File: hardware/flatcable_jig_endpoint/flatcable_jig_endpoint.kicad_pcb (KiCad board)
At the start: 2 copper layers, 2 parts

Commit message: started layout, still need to add the endpad connections
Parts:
- added C1: C, SquantorRcl:C_0805, B.Cu at (111.5, 101.0)
- added C2: C, SquantorRcl:C_0805, B.Cu at (111.5, 108.0)
- added J3: Conn_01x03, Connector_Molex:Molex_KK-254_AE-6410-03A_1x03_P2.54mm_Vertical, F.Cu at (109.0, 104.0)
- added J4: Conn_01x03, Connector_Molex:Molex_KK-254_AE-6410-03A_1x03_P2.54mm_Vertical, F.Cu at (109.0, 111.0)
- added J5: Conn_02x05_Odd_Even, SquantorConnectors:Header-0254-2X05-H010, F.Cu at (126.0, 111.0)
- added R1: R, SquantorRcl:R_0603_hand, B.Cu at (117.0, 111.2)
- added R2: R, SquantorRcl:R_0603_hand, B.Cu at (117.0, 114.2)
- added R3: R, SquantorRcl:R_0603_hand, B.Cu at (117.0, 117.2)
- added R4: R, SquantorRcl:R_0603_hand, B.Cu at (119.5, 110.8)
- added R5: R, SquantorRcl:R_0603_hand, B.Cu at (119.5, 113.8)
- added R6: R, SquantorRcl:R_0603_hand, B.Cu at (119.5, 116.8)
- added R7: R, SquantorRcl:R_0603_hand, B.Cu at (122.0, 111.2)
- added R8: R, SquantorRcl:R_0603_hand, B.Cu at (122.0, 114.2)
- added R9: R, SquantorRcl:R_0603_hand, B.Cu at (122.0, 117.2)
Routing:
- added copper zone on F.Cu, net GND
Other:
- board outline added: 30 x 22 mm

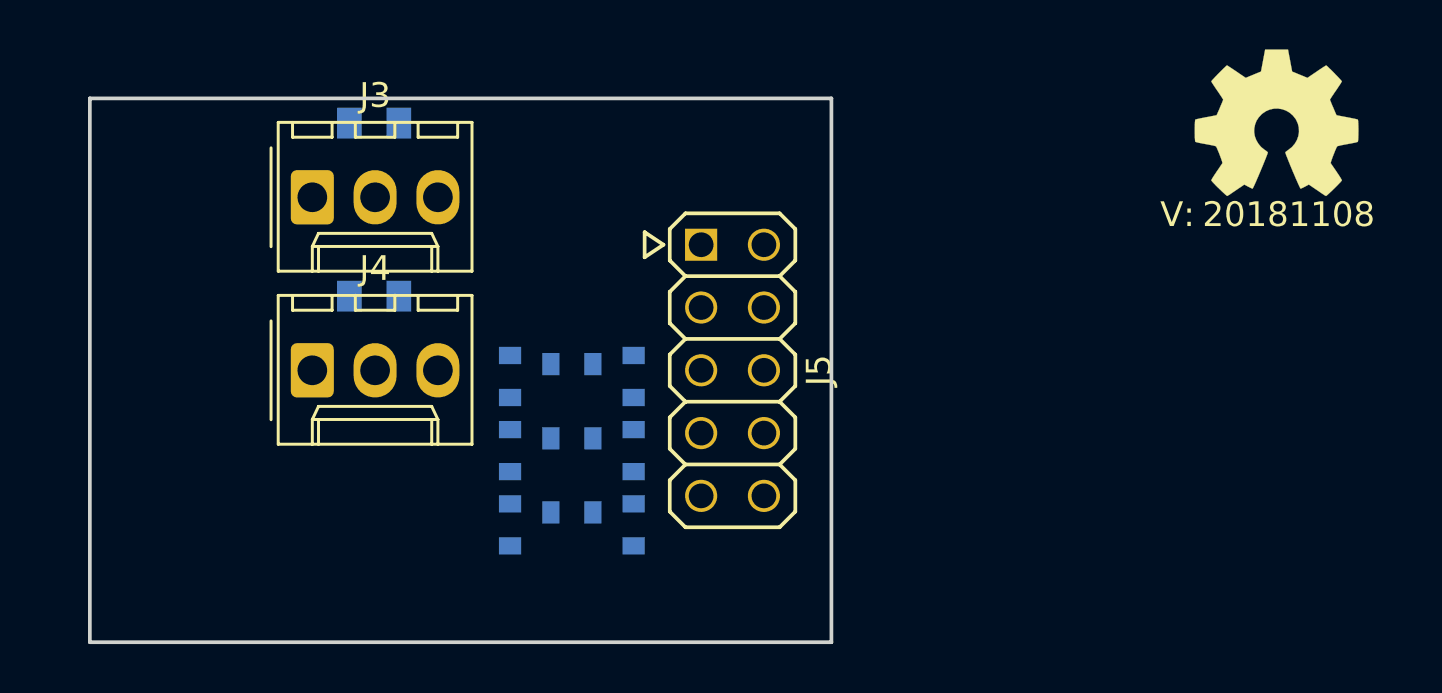
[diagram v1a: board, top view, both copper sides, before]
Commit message: layout completed, now silk screen
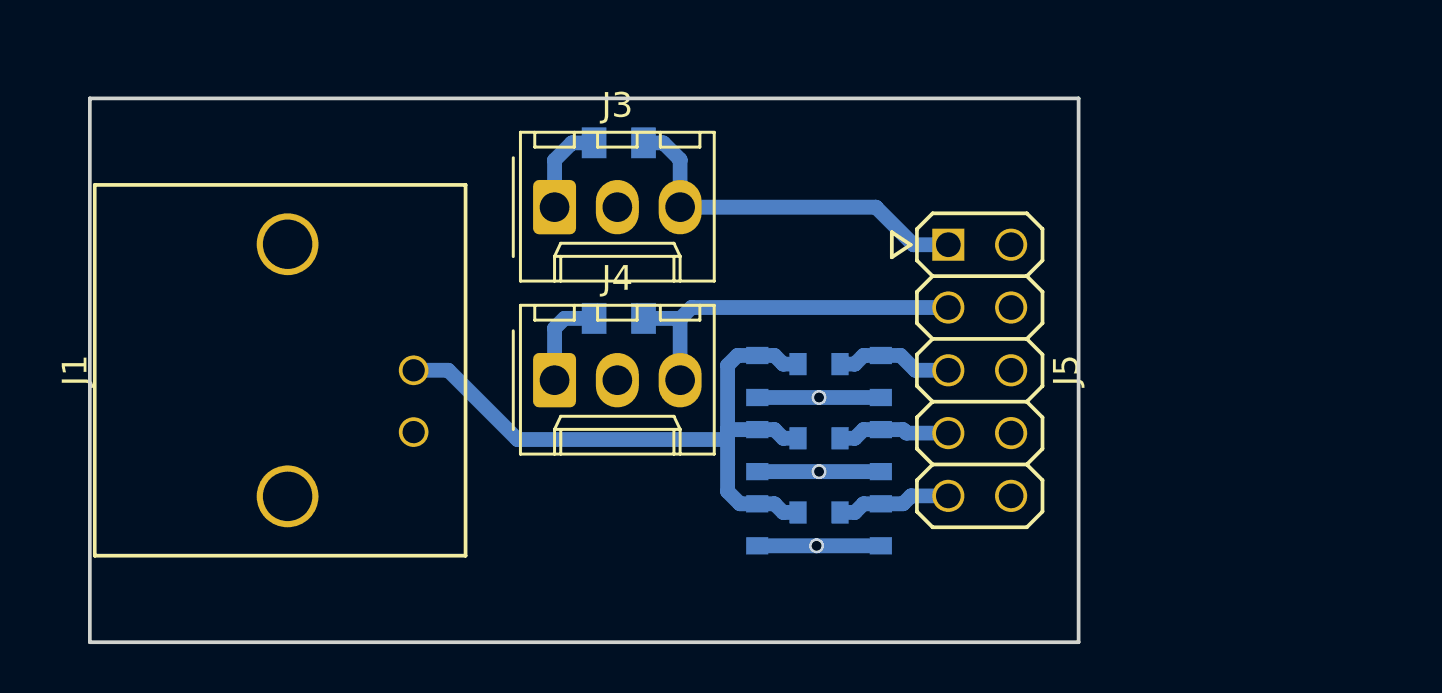
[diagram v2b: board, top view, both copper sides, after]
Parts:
- added J1: Coax, SquantorConnectors:Conn_BNC_RightAngle_TH, F.Cu at (108.0, 111.0)
- N1: moved to B.Cu
- moved J5 10.0 mm to (136.0, 111.0)
- moved R1 10.0 mm to (127.0, 111.2)
- moved R2 10.0 mm to (127.0, 114.2)
- moved R3 10.0 mm to (127.0, 117.2)
- moved R4 10.0 mm to (129.5, 110.8)
- moved R5 10.0 mm to (129.5, 113.8)
- moved R6 10.0 mm to (129.5, 116.8)
- moved R7 10.0 mm to (132.0, 111.2)
- moved R8 10.0 mm to (132.0, 114.2)
- moved R9 10.0 mm to (132.0, 117.2)
- moved C2 9.94 mm to (121.4, 108.9)
- moved C1 9.93 mm to (121.4, 101.8)
- moved J3 9.81 mm to (118.8, 104.4)
- moved J4 9.81 mm to (118.8, 111.4)
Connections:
- J3 pad 2: (no net) -> Net-(J3-Pad2)
- J4 pad 2: (no net) -> Net-(J4-Pad2)
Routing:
- net /SIGNAL: track 0.00 -> 28.1 mm
- net GND: track 0.00 -> 22.7 mm, vias 0 -> 3
- net /POWER_0: track 0.00 -> 15.2 mm
- net /POWER_1: track 0.00 -> 15.0 mm
- net /SIGNAL_0: track 0.00 -> 4.77 mm
- net /SIGNAL_2: track 0.00 -> 4.66 mm
- net /SIGNAL_1: track 0.00 -> 4.58 mm
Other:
- board size 30 x 22 mm -> 40 x 22 mm
- rule pad_to_mask_clearance: 0.2 -> 0.1
- rule solder_mask_min_width: 0.25 -> 0.1

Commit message: updated silkscreen position
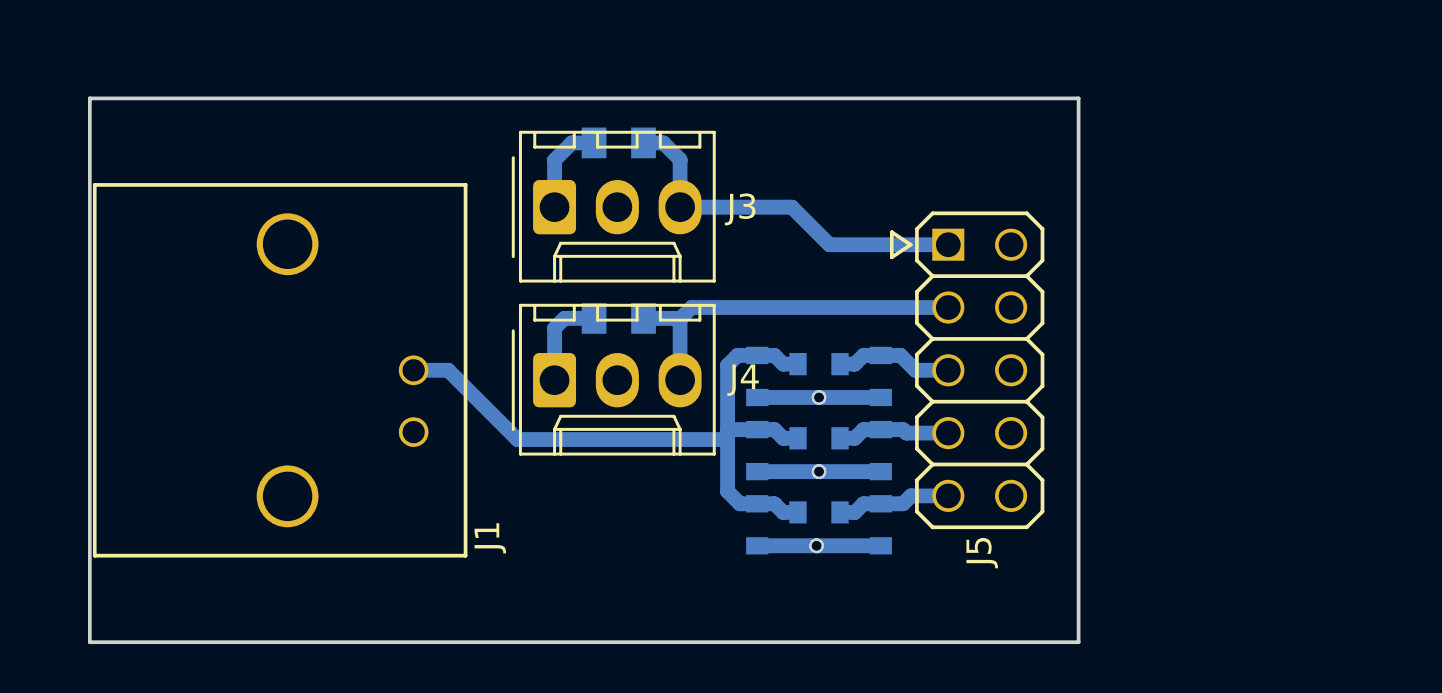
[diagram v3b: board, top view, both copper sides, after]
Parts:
- moved N1 42.9 mm to (106.3, 111.1), turned to 270 degrees
- moved N2 39.3 mm to (110.0, 110.5), turned to 270 degrees
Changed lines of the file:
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@@
   )
   (module Symbols:OSHW-Symbol_6.7x6mm_SilkScreen (layer B.Cu)
-    (at 148 101)
+    (at 106.322036 111.073376 270)
     (descr "Open Source Hardware Symbol")
     (tags "Logo Symbol OSHW")
     (attr virtual)
-    (fp_text reference N1 (at 0 0) (layer B.SilkS) hide
-      (effects (font (size 1 1) (thickness 0.15)) (justify mirror))
-    )
-    (fp_text value OHWLOGO (at 0.75 0) (layer B.Fab) hide
+    (fp_text reference N1 (at 0 0 270) (layer B.SilkS) hide
+      (effects (font (size 1 1) (thickness 0.15)) (justify mirror))
+    )
+    (fp_text value OHWLOGO (at 0.75 0 270) (layer B.Fab) hide
       (effects (font (size 1 1) (thickness 0.15)) (justify mirror))
     )
@@
   )
   (module SquantorLabels:Label_version (layer F.Cu)
-    (at 148.9 104.8)
-    (fp_text reference N2 (at 0 1.4) (layer F.Fab) hide
-      (effects (font (size 1 1) (thickness 0.15)))
-    )
-    (fp_text value 20181108 (at -0.4 -0.1) (layer B.SilkS)
-      (effects (font (size 1 1) (thickness 0.15)) (justify mirror))
-    )
-    (fp_text user V: (at 4.1 -0.2) (layer B.SilkS)
+    (at 110.022036 110.473376 270)
+    (fp_text reference N2 (at 0 1.4 270) (layer F.Fab) hide
+      (effects (font (size 1 1) (thickness 0.15)))
+    )
+    (fp_text value 20181108 (at -0.4 -0.1 270) (layer B.SilkS)
+      (effects (font (size 1 1) (thickness 0.15)) (justify mirror))
+    )
+    (fp_text user V: (at 4.1 -0.1 270) (layer B.SilkS)
       (effects (font (size 1 1) (thickness 0.15)) (justify mirror))
     )
@@
     (tags "capacitor 0805")
     (attr smd)
-    (fp_text reference C1 (at 0 2.1 180) (layer B.SilkS)
+    (fp_text reference C1 (at -2.7 0 180) (layer B.SilkS)
       (effects (font (size 1 1) (thickness 0.15)) (justify mirror))
     )
@@
     (tags "capacitor 0805")
     (attr smd)
-    (fp_text reference C2 (at -0.1 2 180) (layer B.SilkS)
+    (fp_text reference C2 (at -2.8 0 180) (layer B.SilkS)
       (effects (font (size 1 1) (thickness 0.15)) (justify mirror))
     )
@@
     (descr "Molex KK-254 Interconnect System, old/engineering part number: AE-6410-03A example for new part number: 22-27-2031, 3 Pins (http://www.molex.com/pdm_docs/sd/022272021_sd.pdf), generated with kicad-footprint-generator")
     (tags "connector Molex KK-254 side entry")
-    (fp_text reference J3 (at 2.54 -4.12) (layer F.SilkS)
-      (effects (font (size 1 1) (thickness 0.15)))
-    )
-    (fp_text value Conn_01x03 (at 2.54 4.08) (layer F.Fab)
+    (fp_text reference J3 (at 7.6 0) (layer F.SilkS)
+      (effects (font (size 1 1) (thickness 0.15)))
+    )
+    (fp_text value Conn_01x03 (at 2.5 2.2) (layer F.Fab)
       (effects (font (size 1 1) (thickness 0.15)))
     )
@@
     (descr "Molex KK-254 Interconnect System, old/engineering part number: AE-6410-03A example for new part number: 22-27-2031, 3 Pins (http://www.molex.com/pdm_docs/sd/022272021_sd.pdf), generated with kicad-footprint-generator")
     (tags "connector Molex KK-254 side entry")
-    (fp_text reference J4 (at 2.54 -4.12) (layer F.SilkS)
-      (effects (font (size 1 1) (thickness 0.15)))
-    )
-    (fp_text value Conn_01x03 (at 2.54 4.08) (layer F.Fab)
+    (fp_text reference J4 (at 7.7 -0.1) (layer F.SilkS)
+      (effects (font (size 1 1) (thickness 0.15)))
+    )
+    (fp_text value Conn_01x03 (at 2.5 2.1) (layer F.Fab)
       (effects (font (size 1 1) (thickness 0.15)))
     )
@@
     (tags "PIN HEADER")
     (attr virtual)
-    (fp_text reference J5 (at 0 -3.5 270) (layer F.SilkS)
-      (effects (font (size 1 1) (thickness 0.15)))
-    )
-    (fp_text value Conn_02x05_Odd_Even (at 0 3.81 270) (layer F.Fab)
+    (fp_text reference J5 (at 7.3 0 270) (layer F.SilkS)
+      (effects (font (size 1 1) (thickness 0.15)))
+    )
+    (fp_text value Conn_02x05_Odd_Even (at 0 -3.1 270) (layer F.Fab)
       (effects (font (size 1 1) (thickness 0.15)))
     )
@@
     (tags "resistor 0603")
     (attr smd)
-    (fp_text reference R1 (at 2.5 0 90) (layer B.SilkS)
-      (effects (font (size 1 1) (thickness 0.15)) (justify mirror))
-    )
-    (fp_text value R (at 0 -1.9 90) (layer B.Fab)
+    (fp_text reference R1 (at -0.15 -1.4 90) (layer B.SilkS)
+      (effects (font (size 1 1) (thickness 0.15)) (justify mirror))
+    )
+    (fp_text value R (at 0 -1.4 90) (layer B.Fab)
       (effects (font (size 1 1) (thickness 0.15)) (justify mirror))
     )
@@
     (tags "resistor 0603")
     (attr smd)
-    (fp_text reference R2 (at 0.25 -1.5 90) (layer B.SilkS)
-      (effects (font (size 1 1) (thickness 0.15)) (justify mirror))
-    )
-    (fp_text value R (at 0 -1.9 90) (layer B.Fab)
+    (fp_text reference R2 (at 0.05 -1.4 90) (layer B.SilkS)
+      (effects (font (size 1 1) (thickness 0.15)) (justify mirror))
+    )
+    (fp_text value R (at 0.05 -1.4 90) (layer B.Fab)
       (effects (font (size 1 1) (thickness 0.15)) (justify mirror))
     )
@@
     (tags "resistor 0603")
     (attr smd)
-    (fp_text reference R3 (at 0.25 -1.5 90) (layer B.SilkS)
-      (effects (font (size 1 1) (thickness 0.15)) (justify mirror))
-    )
-    (fp_text value R (at 0 -1.9 90) (layer B.Fab)
+    (fp_text reference R3 (at -0.05 -1.4 90) (layer B.SilkS)
+      (effects (font (size 1 1) (thickness 0.15)) (justify mirror))
+    )
+    (fp_text value R (at -0.05 -1.4 90) (layer B.Fab)
       (effects (font (size 1 1) (thickness 0.15)) (justify mirror))
     )
@@
     (tags "resistor 0603")
     (attr smd)
-    (fp_text reference R4 (at 0 1.9 180) (layer B.SilkS)
+    (fp_text reference R4 (at 0 -1.45 180) (layer B.SilkS)
       (effects (font (size 1 1) (thickness 0.15)) (justify mirror))
     )
@@
     (tags "resistor 0603")
     (attr smd)
-    (fp_text reference R5 (at 0 1.9 180) (layer B.SilkS)
-      (effects (font (size 1 1) (thickness 0.15)) (justify mirror))
-    )
-    (fp_text value R (at 0 -1.9 180) (layer B.Fab)
+    (fp_text reference R5 (at 0 -1.55 180) (layer B.SilkS)
+      (effects (font (size 1 1) (thickness 0.15)) (justify mirror))
+    )
+    (fp_text value R (at 0 -1.55 180) (layer B.Fab)
       (effects (font (size 1 1) (thickness 0.15)) (justify mirror))
     )
@@
     (tags "resistor 0603")
     (attr smd)
-    (fp_text reference R6 (at 0 1.9 180) (layer B.SilkS)
-      (effects (font (size 1 1) (thickness 0.15)) (justify mirror))
-    )
-    (fp_text value R (at 0 -1.9 180) (layer B.Fab)
+    (fp_text reference R6 (at 0 -1.55 180) (layer B.SilkS)
+      (effects (font (size 1 1) (thickness 0.15)) (justify mirror))
+    )
+    (fp_text value R (at 0 -1.55 180) (layer B.Fab)
       (effects (font (size 1 1) (thickness 0.15)) (justify mirror))
     )
@@
     (tags "resistor 0603")
     (attr smd)
-    (fp_text reference R7 (at 0 1.9 90) (layer B.SilkS)
-      (effects (font (size 1 1) (thickness 0.15)) (justify mirror))
-    )
-    (fp_text value R (at 0 -1.9 90) (layer B.Fab)
+    (fp_text reference R7 (at 0 1.5 90) (layer B.SilkS)
+      (effects (font (size 1 1) (thickness 0.15)) (justify mirror))
+    )
+    (fp_text value R (at 0 1.5 90) (layer B.Fab)
       (effects (font (size 1 1) (thickness 0.15)) (justify mirror))
     )
@@
     (tags "resistor 0603")
     (attr smd)
-    (fp_text reference R8 (at 0 1.9 90) (layer B.SilkS)
-      (effects (font (size 1 1) (thickness 0.15)) (justify mirror))
-    )
-    (fp_text value R (at 0 -1.9 90) (layer B.Fab)
+    (fp_text reference R8 (at 0 1.5 90) (layer B.SilkS)
+      (effects (font (size 1 1) (thickness 0.15)) (justify mirror))
+    )
+    (fp_text value R (at 0 1.5 90) (layer B.Fab)
       (effects (font (size 1 1) (thickness 0.15)) (justify mirror))
     )
@@
     (tags "resistor 0603")
     (attr smd)
-    (fp_text reference R9 (at 0 1.9 90) (layer B.SilkS)
-      (effects (font (size 1 1) (thickness 0.15)) (justify mirror))
-    )
-    (fp_text value R (at 0 -1.9 90) (layer B.Fab)
+    (fp_text reference R9 (at -0.05 1.5 90) (layer B.SilkS)
+      (effects (font (size 1 1) (thickness 0.15)) (justify mirror))
+    )
+    (fp_text value R (at -0.05 1.5 90) (layer B.Fab)
       (effects (font (size 1 1) (thickness 0.15)) (justify mirror))
     )
@@
   (module SquantorConnectors:Conn_BNC_RightAngle_TH (layer F.Cu)
     (at 108 111 90)
-    (fp_text reference J1 (at 0 -8.6 90) (layer F.SilkS)
+    (fp_text reference J1 (at -6.7 8.1 90) (layer F.SilkS)
       (effects (font (size 1 1) (thickness 0.15)))
     )
@@
   (segment (start 127 112.1) (end 129.5 112.1) (width 0.6) (layer B.Cu) (net 1))
   (segment (start 132 112.1) (end 129.5 112.1) (width 0.6) (layer B.Cu) (net 1))
-  (segment (start 134.73 105.92) (end 133.32 105.92) (width 0.6) (layer B.Cu) (net 2))
-  (segment (start 131.8 104.4) (end 123.88 104.4) (width 0.6) (layer B.Cu) (net 2))
-  (segment (start 133.32 105.92) (end 131.8 104.4) (width 0.6) (layer B.Cu) (net 2))
   (segment (start 122.4 101.8) (end 123.2 101.8) (width 0.6) (layer B.Cu) (net 2))
   (segment (start 123.88 102.48) (end 123.88 104.4) (width 0.6) (layer B.Cu) (net 2))
   (segment (start 123.2 101.8) (end 123.88 102.48) (width 0.6) (layer B.Cu) (net 2))
+  (segment (start 128.4 104.4) (end 123.88 104.4) (width 0.6) (layer B.Cu) (net 2))
+  (segment (start 134.73 105.92) (end 129.92 105.92) (width 0.6) (layer B.Cu) (net 2))
+  (segment (start 129.92 105.92) (end 128.4 104.4) (width 0.6) (layer B.Cu) (net 2))
   (segment (start 134.73 108.46) (end 124.34 108.46) (width 0.6) (layer B.Cu) (net 3))
   (segment (start 123.9 108.9) (end 122.4 108.9) (width 0.6) (layer B.Cu) (net 3))

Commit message: updated versionnumber, adjusted cutout line thickness to 0.1mm
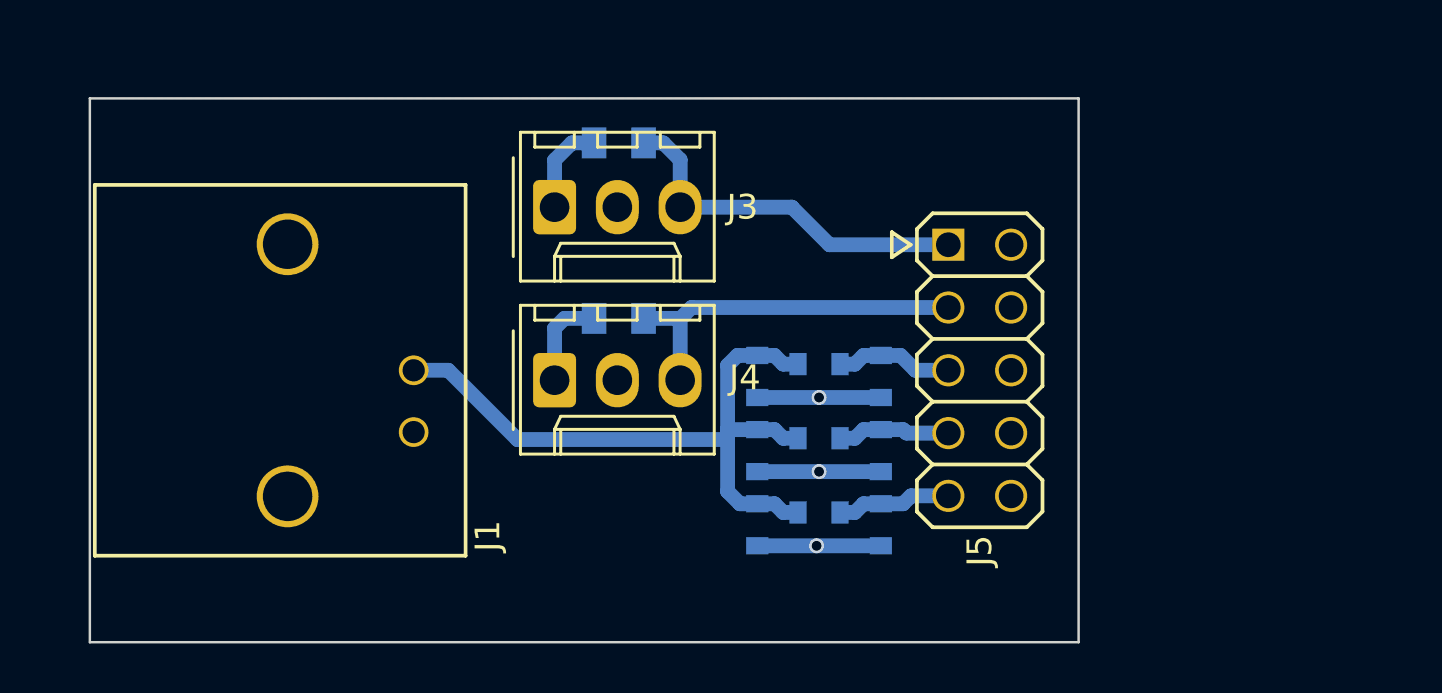
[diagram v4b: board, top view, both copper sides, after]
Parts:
- N2: value 20181108 -> 20181216
- moved N2 1.83 mm to (110.1, 112.3)
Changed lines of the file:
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@@
   )
   (setup
-    (last_trace_width 0.6)
+    (last_trace_width 0.1524)
     (user_trace_width 0.1524)
     (user_trace_width 0.2)
@@
     (trace_min 0.1524)
     (segment_width 0.2)
-    (edge_width 0.15)
+    (edge_width 0.1)
     (via_size 0.381)
     (via_drill 0.254)
@@
   )
   (module SquantorLabels:Label_version (layer F.Cu)
-    (at 110.022036 110.473376 270)
+    (at 110.1 112.3 270)
     (fp_text reference N2 (at 0 1.4 270) (layer F.Fab) hide
       (effects (font (size 1 1) (thickness 0.15)))
     )
-    (fp_text value 20181108 (at -0.4 -0.1 270) (layer B.SilkS)
-      (effects (font (size 1 1) (thickness 0.15)) (justify mirror))
-    )
-    (fp_text user V: (at 4.1 -0.1 270) (layer B.SilkS)
+    (fp_text value 20181216 (at -0.4 -0.1 270) (layer B.SilkS)
+      (effects (font (size 1 1) (thickness 0.15)) (justify mirror))
+    )
+    (fp_text user V: (at -4.873376 -0.077964 270) (layer B.SilkS)
       (effects (font (size 1 1) (thickness 0.15)) (justify mirror))
     )
@@
       (net 1 GND))
   )
-  (gr_line (start 140 122) (end 100 122) (layer Edge.Cuts) (width 0.15))
-  (gr_line (start 100 100) (end 140 100) (layer Edge.Cuts) (width 0.15))
-  (gr_line (start 140 100) (end 140 122) (layer Edge.Cuts) (width 0.15))
-  (gr_line (start 100 100) (end 100 122) (layer Edge.Cuts) (width 0.15))
+  (gr_line (start 140 122) (end 100 122) (layer Edge.Cuts) (width 0.1))
+  (gr_line (start 100 100) (end 140 100) (layer Edge.Cuts) (width 0.1))
+  (gr_line (start 140 100) (end 140 122) (layer Edge.Cuts) (width 0.1))
+  (gr_line (start 100 100) (end 100 122) (layer Edge.Cuts) (width 0.1))
   (segment (start 118.8 102.5) (end 118.8 104.4) (width 0.6) (layer B.Cu) (net 1))
   (segment (start 120.4 101.8) (end 119.5 101.8) (width 0.6) (layer B.Cu) (net 1))
